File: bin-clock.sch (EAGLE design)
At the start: 4 parts

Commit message: current working schematic recorded
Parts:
- added C1: (no value), capacitor-wima:C2,5-3
- added IC1: 4060N, 40xx:4060N
- added Q1: 32.768 Khz, crystal:CRYSTAL68SMX
- added R4: 10 M, rcl:R-US_0204/2V
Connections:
- net N$3 renamed POS-V-IC1
- new net GND: C1.1, IC1A.RES
- new net N$4: IC1A.Q14
- new net N$5: C1.2, IC1A.!P0, Q1.1, R4.1
- new net N$6: IC1A.P1, Q1.2, R4.2
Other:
- note added: "16"
- note added: "2 Hz"
- note added: "8"
- moved on the sheet: BATTERY, R1, R2, R3
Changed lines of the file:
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@@
 <part name="R2" library="resistor" deviceset="R-US_" device="0204/2V" value="2K"/>
 <part name="R3" library="resistor" deviceset="R-US_" device="0204/2V" value="3K"/>
+<part name="IC1" library="40xx" deviceset="4060" device="N"/>
+<part name="R4" library="rcl" deviceset="R-US_" device="0204/2V" value="10 M"/>
+<part name="C1" library="capacitor-wima" deviceset="C" device="2,5-3"/>
+<part name="SUPPLY1" library="supply2" deviceset="GND" device=""/>
+<part name="SUPPLY2" library="supply2" deviceset="GND" device=""/>
+<part name="Q1" library="crystal" deviceset="CRYSTAL" device="68SMX" value="32.768 Khz"/>
 </parts>
 <sheets>
 <sheet>
 <plain>
+<text x="-2.54" y="104.14" size="1.778" layer="91">16</text>
+<text x="0.762" y="63.246" size="1.778" layer="91">8</text>
+<text x="25.4" y="73.66" size="1.778" layer="91">2 Hz</text>
 </plain>
 <instances>
-<instance part="BATTERY" gate="G$1" x="-7.62" y="60.96" rot="R90"/>
-<instance part="R1" gate="G$1" x="15.24" y="78.74"/>
-<instance part="R2" gate="G$1" x="15.24" y="43.18"/>
-<instance part="R3" gate="G$1" x="35.56" y="25.4"/>
+<instance part="BATTERY" gate="G$1" x="-91.44" y="99.06" rot="R90"/>
+<instance part="R1" gate="G$1" x="-68.58" y="116.84"/>
+<instance part="R2" gate="G$1" x="-68.58" y="81.28"/>
+<instance part="R3" gate="G$1" x="-66.04" y="63.5"/>
+<instance part="IC1" gate="A" x="-2.54" y="83.82"/>
+<instance part="R4" gate="G$1" x="-35.56" y="81.28" rot="R90"/>
+<instance part="C1" gate="G$1" x="-30.48" y="66.04" rot="R270"/>
+<instance part="SUPPLY1" gate="GND" x="-27.94" y="66.04" rot="R90"/>
+<instance part="SUPPLY2" gate="GND" x="-17.78" y="68.58" rot="R270"/>
+<instance part="Q1" gate="G$1" x="-43.18" y="73.66" rot="R180"/>
 </instances>
 <busses>
@@
 <segment>
 <pinref part="R2" gate="G$1" pin="1"/>
-<wire x1="2.54" y1="43.18" x2="10.16" y2="43.18" width="0.1524" layer="91"/>
-<wire x1="2.54" y1="43.18" x2="2.54" y2="25.4" width="0.1524" layer="91"/>
-<wire x1="2.54" y1="25.4" x2="30.48" y2="25.4" width="0.1524" layer="91"/>
+<wire x1="-81.28" y1="81.28" x2="-73.66" y2="81.28" width="0.1524" layer="91"/>
+<wire x1="-81.28" y1="81.28" x2="-81.28" y2="63.5" width="0.1524" layer="91"/>
+<wire x1="-81.28" y1="63.5" x2="-71.12" y2="63.5" width="0.1524" layer="91"/>
 <pinref part="R3" gate="G$1" pin="1"/>
 <pinref part="BATTERY" gate="G$1" pin="-"/>
-<wire x1="-7.62" y1="48.26" x2="-7.62" y2="43.18" width="0.1524" layer="91"/>
-<wire x1="-7.62" y1="43.18" x2="2.54" y2="43.18" width="0.1524" layer="91"/>
-<junction x="2.54" y="43.18"/>
+<wire x1="-91.44" y1="86.36" x2="-91.44" y2="81.28" width="0.1524" layer="91"/>
+<wire x1="-91.44" y1="81.28" x2="-81.28" y2="81.28" width="0.1524" layer="91"/>
+<junction x="-81.28" y="81.28"/>
 </segment>
 </net>
-<net name="N$3" class="0">
+<net name="POS-V-IC1" class="0">
 <segment>
 <pinref part="R1" gate="G$1" pin="2"/>
 <pinref part="R2" gate="G$1" pin="2"/>
-<wire x1="20.32" y1="78.74" x2="20.32" y2="60.96" width="0.1524" layer="91"/>
-<junction x="20.32" y="60.96"/>
-<wire x1="20.32" y1="60.96" x2="20.32" y2="43.18" width="0.1524" layer="91"/>
-<wire x1="20.32" y1="60.96" x2="63.5" y2="60.96" width="0.1524" layer="91"/>
+<wire x1="-63.5" y1="116.84" x2="-63.5" y2="99.06" width="0.1524" layer="91"/>
+<junction x="-63.5" y="99.06"/>
+<wire x1="-63.5" y1="99.06" x2="-63.5" y2="81.28" width="0.1524" layer="91"/>
+<wire x1="-63.5" y1="99.06" x2="-43.18" y2="99.06" width="0.1524" layer="91"/>
+<wire x1="-43.18" y1="99.06" x2="-43.18" y2="116.84" width="0.1524" layer="91"/>
+<wire x1="-43.18" y1="116.84" x2="-2.54" y2="116.84" width="0.1524" layer="91"/>
+<wire x1="-2.54" y1="116.84" x2="-2.54" y2="101.6" width="0.1524" layer="91"/>
 </segment>
 </net>
@@
 <segment>
 <pinref part="BATTERY" gate="G$1" pin="+"/>
-<wire x1="-7.62" y1="73.66" x2="-7.62" y2="78.74" width="0.1524" layer="91"/>
+<wire x1="-91.44" y1="111.76" x2="-91.44" y2="116.84" width="0.1524" layer="91"/>
 <pinref part="R1" gate="G$1" pin="1"/>
-<wire x1="-7.62" y1="78.74" x2="10.16" y2="78.74" width="0.1524" layer="91"/>
+<wire x1="-91.44" y1="116.84" x2="-73.66" y2="116.84" width="0.1524" layer="91"/>
+</segment>
+</net>
+<net name="N$3" class="0">
+<segment>
+<pinref part="R3" gate="G$1" pin="2"/>
+<wire x1="-60.96" y1="63.5" x2="-43.18" y2="63.5" width="0.1524" layer="91"/>
+<wire x1="-43.18" y1="63.5" x2="-43.18" y2="35.56" width="0.1524" layer="91"/>
+<wire x1="-43.18" y1="35.56" x2="0" y2="35.56" width="0.1524" layer="91"/>
+<wire x1="0" y1="35.56" x2="0" y2="66.04" width="0.1524" layer="91"/>
 </segment>
 </net>
 <net name="N$4" class="0">
 <segment>
-<pinref part="R3" gate="G$1" pin="2"/>
-<wire x1="40.64" y1="25.4" x2="63.5" y2="25.4" width="0.1524" layer="91"/>
+<pinref part="IC1" gate="A" pin="Q14"/>
+<wire x1="10.16" y1="76.2" x2="43.18" y2="76.2" width="0.1524" layer="91"/>
 </segment>
 </net>
+<net name="N$5" class="0">
+<segment>
+<pinref part="IC1" gate="A" pin="!P0"/>
+<wire x1="10.16" y1="68.58" x2="12.7" y2="68.58" width="0.1524" layer="91"/>
+<wire x1="12.7" y1="68.58" x2="12.7" y2="53.34" width="0.1524" layer="91"/>
+<wire x1="12.7" y1="53.34" x2="-35.56" y2="53.34" width="0.1524" layer="91"/>
+<wire x1="-35.56" y1="53.34" x2="-35.56" y2="66.04" width="0.1524" layer="91"/>
+<pinref part="C1" gate="G$1" pin="2"/>
+<pinref part="R4" gate="G$1" pin="1"/>
+<wire x1="-35.56" y1="76.2" x2="-35.56" y2="73.66" width="0.1524" layer="91"/>
+<pinref part="Q1" gate="G$1" pin="1"/>
+<wire x1="-35.56" y1="73.66" x2="-35.56" y2="66.04" width="0.1524" layer="91"/>
+<wire x1="-40.64" y1="73.66" x2="-35.56" y2="73.66" width="0.1524" layer="91"/>
+<junction x="-35.56" y="73.66"/>
+<junction x="-35.56" y="66.04"/>
+</segment>
+</net>
+<net name="GND" class="0">
+<segment>
+<pinref part="C1" gate="G$1" pin="1"/>
+<pinref part="SUPPLY1" gate="GND" pin="GND"/>
+<wire x1="-30.48" y1="66.04" x2="-27.94" y2="66.04" width="0.1524" layer="91"/>
+</segment>
+<segment>
+<pinref part="IC1" gate="A" pin="RES"/>
+<pinref part="SUPPLY2" gate="GND" pin="GND"/>
+</segment>
+</net>
+<net name="N$6" class="0">
+<segment>
+<pinref part="Q1" gate="G$1" pin="2"/>
+<wire x1="-45.72" y1="73.66" x2="-45.72" y2="86.36" width="0.1524" layer="91"/>
+<pinref part="R4" gate="G$1" pin="2"/>
+<wire x1="-45.72" y1="86.36" x2="-35.56" y2="86.36" width="0.1524" layer="91"/>
+<wire x1="-35.56" y1="86.36" x2="-35.56" y2="99.06" width="0.1524" layer="91"/>
+<pinref part="IC1" gate="A" pin="P1"/>
+<wire x1="-35.56" y1="99.06" x2="-15.24" y2="99.06" width="0.1524" layer="91"/>
+</segment>
+</net>

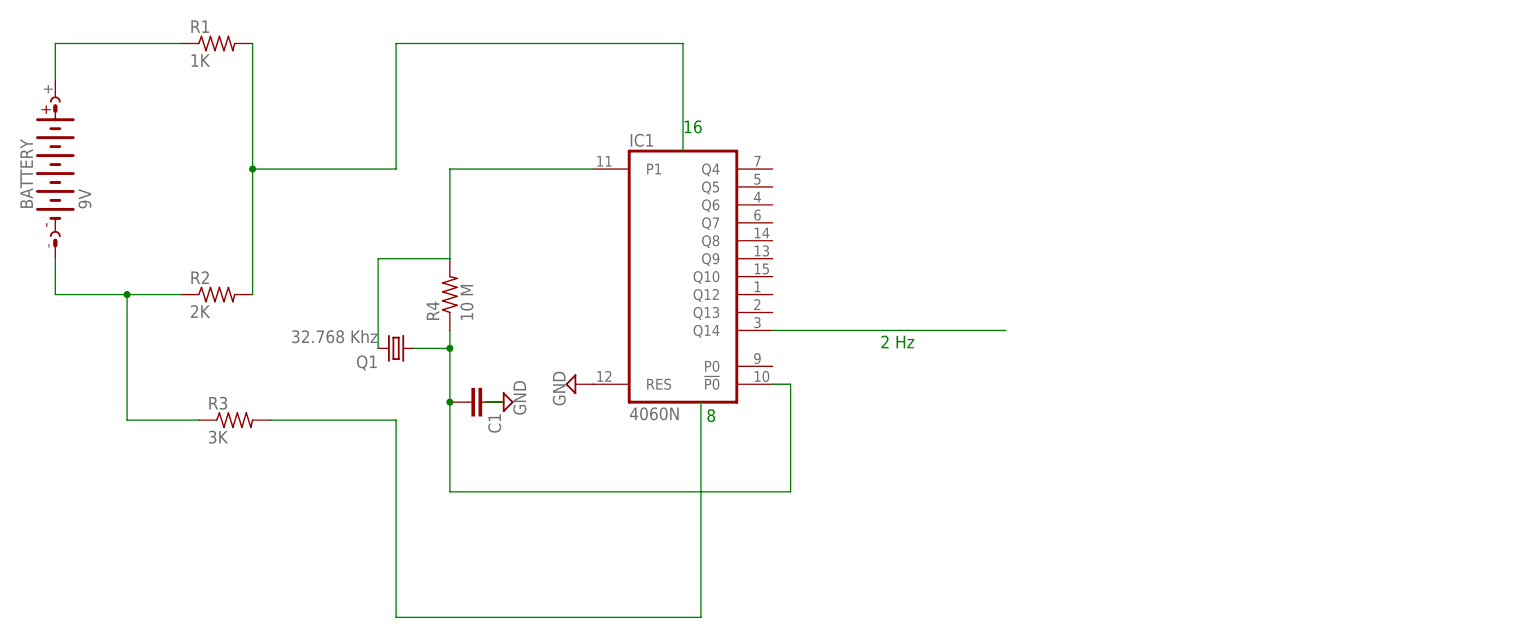
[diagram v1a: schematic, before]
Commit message: add seconds logic
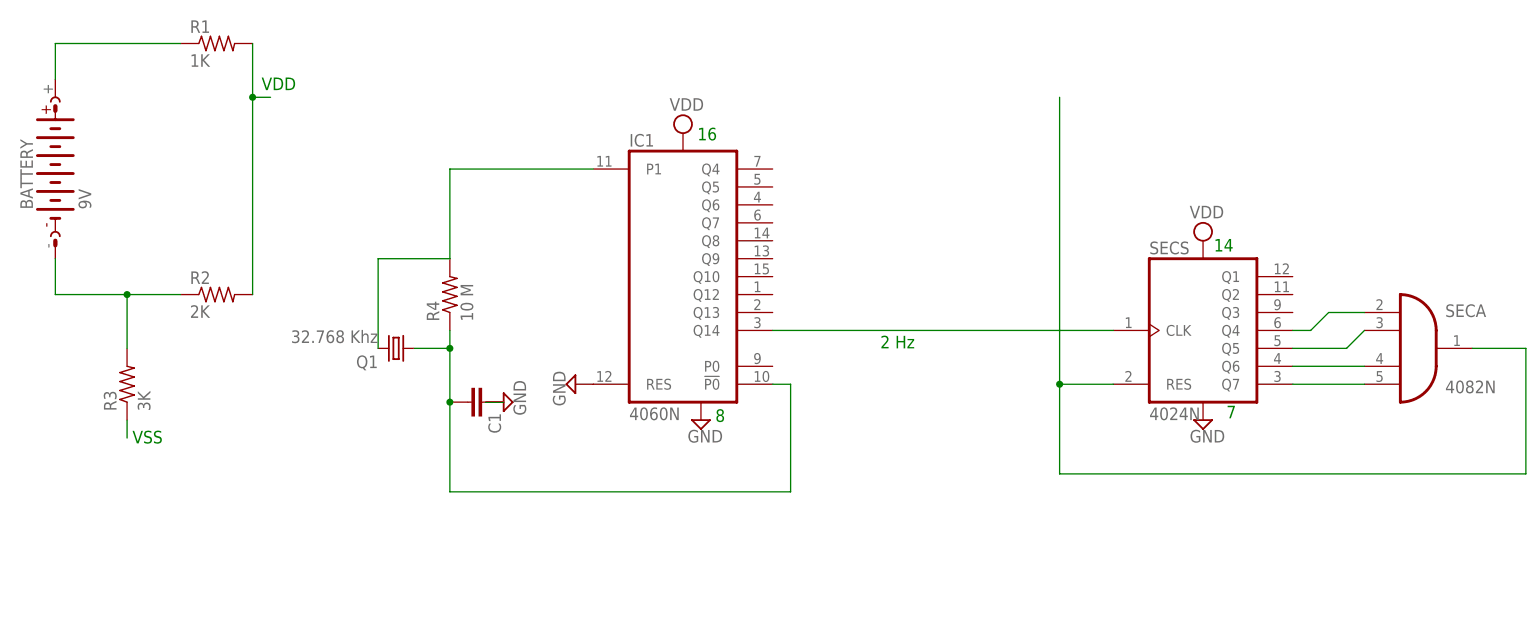
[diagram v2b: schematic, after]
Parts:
- added SEC: 4082N, 40xx:4082N
- added SECS: 4024N, 40xx:4024N
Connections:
- net POS-V-IC1 renamed N$7
- new net N$10: SECA.I2, SECSA.Q6
- new net N$11: SECA.I3, SECSA.Q7
- new net N$12: SECA.O, SECSA.RES
- new net N$8: SECA.I0, SECSA.Q4
- new net N$9: SECA.I1, SECSA.Q5
- net N$2: now also R3.2; no longer R3.1
- net N$3: now also R3.1; no longer R3.2
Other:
- note added: "14"
- note added: "7"
- note added: "VDD"
- note added: "VSS"
- moved on the sheet: R3
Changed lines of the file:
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@@
 <part name="SUPPLY2" library="supply2" deviceset="GND" device=""/>
 <part name="Q1" library="crystal" deviceset="CRYSTAL" device="68SMX" value="32.768 Khz"/>
+<part name="SECS" library="40xx" deviceset="4024" device="N"/>
+<part name="SUPPLY3" library="supply2" deviceset="VDD" device=""/>
+<part name="SUPPLY4" library="supply2" deviceset="GND" device=""/>
+<part name="SUPPLY5" library="supply2" deviceset="VDD" device=""/>
+<part name="SUPPLY6" library="supply2" deviceset="GND" device=""/>
+<part name="SEC" library="40xx" deviceset="4082" device="N"/>
 </parts>
 <sheets>
 <sheet>
 <plain>
-<text x="-2.54" y="104.14" size="1.778" layer="91">16</text>
-<text x="0.762" y="63.246" size="1.778" layer="91">8</text>
+<text x="-0.508" y="103.124" size="1.778" layer="91">16</text>
+<text x="2.032" y="63.246" size="1.778" layer="91">8</text>
 <text x="25.4" y="73.66" size="1.778" layer="91">2 Hz</text>
+<text x="-62.23" y="110.236" size="1.778" layer="91">VDD</text>
+<text x="-80.518" y="60.198" size="1.778" layer="91">VSS</text>
+<text x="72.644" y="87.376" size="1.778" layer="91">14</text>
+<text x="74.422" y="63.754" size="1.778" layer="91">7</text>
 </plain>
 <instances>
@@
 <instance part="R1" gate="G$1" x="-68.58" y="116.84"/>
 <instance part="R2" gate="G$1" x="-68.58" y="81.28"/>
-<instance part="R3" gate="G$1" x="-66.04" y="63.5"/>
+<instance part="R3" gate="G$1" x="-81.28" y="68.58" rot="R90"/>
 <instance part="IC1" gate="A" x="-2.54" y="83.82"/>
 <instance part="R4" gate="G$1" x="-35.56" y="81.28" rot="R90"/>
@@
 <instance part="SUPPLY2" gate="GND" x="-17.78" y="68.58" rot="R270"/>
 <instance part="Q1" gate="G$1" x="-43.18" y="73.66" rot="R180"/>
+<instance part="SECS" gate="A" x="71.12" y="76.2"/>
+<instance part="SUPPLY3" gate="G$1" x="-2.54" y="104.14"/>
+<instance part="SUPPLY4" gate="GND" x="0" y="63.5"/>
+<instance part="SUPPLY5" gate="G$1" x="71.12" y="88.9"/>
+<instance part="SUPPLY6" gate="GND" x="71.12" y="63.5"/>
+<instance part="SEC" gate="A" x="101.6" y="73.66"/>
 </instances>
 <busses>
@@
 <pinref part="R2" gate="G$1" pin="1"/>
 <wire x1="-81.28" y1="81.28" x2="-73.66" y2="81.28" width="0.1524" layer="91"/>
-<wire x1="-81.28" y1="81.28" x2="-81.28" y2="63.5" width="0.1524" layer="91"/>
-<wire x1="-81.28" y1="63.5" x2="-71.12" y2="63.5" width="0.1524" layer="91"/>
-<pinref part="R3" gate="G$1" pin="1"/>
+<wire x1="-81.28" y1="81.28" x2="-81.28" y2="73.66" width="0.1524" layer="91"/>
 <pinref part="BATTERY" gate="G$1" pin="-"/>
 <wire x1="-91.44" y1="86.36" x2="-91.44" y2="81.28" width="0.1524" layer="91"/>
 <wire x1="-91.44" y1="81.28" x2="-81.28" y2="81.28" width="0.1524" layer="91"/>
 <junction x="-81.28" y="81.28"/>
-</segment>
-</net>
-<net name="POS-V-IC1" class="0">
-<segment>
-<pinref part="R1" gate="G$1" pin="2"/>
-<pinref part="R2" gate="G$1" pin="2"/>
-<wire x1="-63.5" y1="116.84" x2="-63.5" y2="99.06" width="0.1524" layer="91"/>
-<junction x="-63.5" y="99.06"/>
-<wire x1="-63.5" y1="99.06" x2="-63.5" y2="81.28" width="0.1524" layer="91"/>
-<wire x1="-63.5" y1="99.06" x2="-43.18" y2="99.06" width="0.1524" layer="91"/>
-<wire x1="-43.18" y1="99.06" x2="-43.18" y2="116.84" width="0.1524" layer="91"/>
-<wire x1="-43.18" y1="116.84" x2="-2.54" y2="116.84" width="0.1524" layer="91"/>
-<wire x1="-2.54" y1="116.84" x2="-2.54" y2="101.6" width="0.1524" layer="91"/>
+<pinref part="R3" gate="G$1" pin="2"/>
 </segment>
 </net>
@@
 </segment>
 </net>
-<net name="N$3" class="0">
-<segment>
-<pinref part="R3" gate="G$1" pin="2"/>
-<wire x1="-60.96" y1="63.5" x2="-43.18" y2="63.5" width="0.1524" layer="91"/>
-<wire x1="-43.18" y1="63.5" x2="-43.18" y2="35.56" width="0.1524" layer="91"/>
-<wire x1="-43.18" y1="35.56" x2="0" y2="35.56" width="0.1524" layer="91"/>
-<wire x1="0" y1="35.56" x2="0" y2="66.04" width="0.1524" layer="91"/>
-</segment>
-</net>
 <net name="N$4" class="0">
 <segment>
 <pinref part="IC1" gate="A" pin="Q14"/>
-<wire x1="10.16" y1="76.2" x2="43.18" y2="76.2" width="0.1524" layer="91"/>
+<wire x1="10.16" y1="76.2" x2="58.42" y2="76.2" width="0.1524" layer="91"/>
 </segment>
 </net>
@@
 </segment>
 </net>
+<net name="N$7" class="0">
+<segment>
+<pinref part="R1" gate="G$1" pin="2"/>
+<pinref part="R2" gate="G$1" pin="2"/>
+<wire x1="-63.5" y1="116.84" x2="-63.5" y2="109.22" width="0.1524" layer="91"/>
+<wire x1="-63.5" y1="109.22" x2="-63.5" y2="81.28" width="0.1524" layer="91"/>
+<wire x1="-63.5" y1="109.22" x2="-60.96" y2="109.22" width="0.1524" layer="91"/>
+<junction x="-63.5" y="109.22"/>
+</segment>
+</net>
+<net name="N$3" class="0">
+<segment>
+<pinref part="R3" gate="G$1" pin="1"/>
+<wire x1="-81.28" y1="63.5" x2="-81.28" y2="60.96" width="0.1524" layer="91"/>
+</segment>
+</net>
+<net name="N$8" class="0">
+<segment>
+<pinref part="SECS" gate="A" pin="Q4"/>
+<wire x1="83.82" y1="76.2" x2="86.36" y2="76.2" width="0.1524" layer="91"/>
+<wire x1="86.36" y1="76.2" x2="88.9" y2="78.74" width="0.1524" layer="91"/>
+<pinref part="SEC" gate="A" pin="I0"/>
+<wire x1="88.9" y1="78.74" x2="93.98" y2="78.74" width="0.1524" layer="91"/>
+</segment>
+</net>
+<net name="N$9" class="0">
+<segment>
+<pinref part="SECS" gate="A" pin="Q5"/>
+<pinref part="SEC" gate="A" pin="I1"/>
+<wire x1="83.82" y1="73.66" x2="91.44" y2="73.66" width="0.1524" layer="91"/>
+<wire x1="91.44" y1="73.66" x2="93.98" y2="76.2" width="0.1524" layer="91"/>
+</segment>
+</net>
+<net name="N$10" class="0">
+<segment>
+<pinref part="SECS" gate="A" pin="Q6"/>
+<pinref part="SEC" gate="A" pin="I2"/>
+<wire x1="83.82" y1="71.12" x2="93.98" y2="71.12" width="0.1524" layer="91"/>
+</segment>
+</net>
+<net name="N$11" class="0">
+<segment>
+<pinref part="SECS" gate="A" pin="Q7"/>
+<pinref part="SEC" gate="A" pin="I3"/>
+<wire x1="83.82" y1="68.58" x2="93.98" y2="68.58" width="0.1524" layer="91"/>
+</segment>
+</net>
+<net name="N$12" class="0">
+<segment>
+<pinref part="SEC" gate="A" pin="O"/>
+<wire x1="109.22" y1="73.66" x2="116.84" y2="73.66" width="0.1524" layer="91"/>
+<wire x1="116.84" y1="73.66" x2="116.84" y2="55.88" width="0.1524" layer="91"/>
+<wire x1="116.84" y1="55.88" x2="50.8" y2="55.88" width="0.1524" layer="91"/>
+<wire x1="50.8" y1="55.88" x2="50.8" y2="68.58" width="0.1524" layer="91"/>
+<pinref part="SECS" gate="A" pin="RES"/>
+<wire x1="50.8" y1="68.58" x2="50.8" y2="109.22" width="0.1524" layer="91"/>
+<wire x1="58.42" y1="68.58" x2="50.8" y2="68.58" width="0.1524" layer="91"/>
+<junction x="50.8" y="68.58"/>
+</segment>
+</net>

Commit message: finish schematic
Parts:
- added HOUR_ONES, HOUR_TENS, MIN_ONES, MIN_TENS: 4024N, 40xx:4024N
- added HOUR_ONE_, HOUR_TENS_, MIN_ONES_, MIN_TENS_: 4082N, 40xx:4082N
- added LED1, LED10, LED11, LED12, LED13, LED2, LED3, LED4, LED5, LED6, LED7, LED8, LED9: (no value), eagle-ltspice:LED_ELD260
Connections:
- new net N$13: LED1.A, MIN_ONESA.Q1
- new net N$14: HOUR_ONESA.CLK, MIN_TENSA.RES, MIN_TENS_A.O
- new net N$15: LED3.A, MIN_ONESA.Q3
- new net N$16: LED4.A, MIN_ONESA.Q4, MIN_ONES_A.I2
- new net N$17: MIN_ONESA.RES, MIN_ONES_A.O, MIN_TENSA.CLK
- new net N$18: LED5.A, MIN_TENSA.Q1
- new net N$19: LED6.A, MIN_TENSA.Q2, MIN_TENS_A.I0, MIN_TENS_A.I1
- new net N$20: LED7.A, MIN_TENSA.Q3, MIN_TENS_A.I2, MIN_TENS_A.I3
- new net N$21: LED2.A, MIN_ONESA.Q2, MIN_ONES_A.I0, MIN_ONES_A.I1
- new net N$22: HOUR_ONESA.Q1, LED8.A
- new net N$23: HOUR_ONESA.Q2, HOUR_ONE_A.I0, HOUR_ONE_A.I1, LED9.A
- new net N$24: HOUR_ONESA.Q3, HOUR_TENS_A.I2, HOUR_TENS_A.I3, LED10.A
- new net N$25: HOUR_ONESA.Q4, HOUR_ONE_A.I2, HOUR_ONE_A.I3, LED11.A
- new net N$26: HOUR_ONESA.RES, HOUR_ONE_A.O, HOUR_TENSA.CLK
- new net N$27: HOUR_TENSA.Q1, LED12.A
- new net N$28: HOUR_TENSA.Q2, HOUR_TENS_A.I0, HOUR_TENS_A.I1, LED13.A
- new net N$29: HOUR_TENSA.RES, HOUR_TENS_A.O
- net GND: now also LED1.C, LED10.C, LED11.C, LED12.C, LED2.C, LED3.C, LED4.C, LED5.C, LED6.C, LED7.C, LED8.C, LED9.C
- net N$12: now also MIN_ONESA.CLK
